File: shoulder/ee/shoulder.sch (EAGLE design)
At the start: 34 parts, among them IC3 XMEGA-A4, J1(RS) RJ11-6PTH, J2(LS) RJ11-6PTH, T1 2N2222

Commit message: shoulder: schematic updates for new board
- all through hole resistors replaced with 0603
- All through hole capacitors replaced with 0603
- through hole LEDs replaced with SMT
- Added jumpers to switch between SPI and USART peripheral for LED
  controllers
    - USART in SPI master mode allows DMA.
- Added reset button.
- Added a pullup on AVR reset line.
- Moved T1 and BUZZ (JST conn) further from screw holes.
- Moved vibrator further from screw holes.
- Replaced IR receivers with SMT heimdall package
- Added a footprint for a 3rd IR receiver (facing up)
- Replaced through hole NPN transistor with SMT
- Replaced 4 pin ISP with 6 pin 50mil RA header.
- Added frame to schematic :o
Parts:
- removed ISP1: (no value), SparkFun-Connectors:M04LOCK
- added C2: 0.1uF, SparkFun-Capacitors:CAP0603-CAP
- added ISP: PDI, greg:PDI
- added R1: (no value), SparkFun-Resistors:RESISTOR0603-RES
- added RST: SPST_TACT-EVQQ2, adafruit:SPST_TACT-EVQQ2
- added SJ1, SJ2: (no value), SparkFun-Passives:SOLDERJUMPER_2WAYT
- added U$3: TSMP77000UP, greg:TSMP77000UP
- C24, C25, C3, C4: device SparkFun-Passives:CAPPTH -> SparkFun-Capacitors:CAP0603-CAP
- R18, R19, R3, R4: device adafruit:R-US_0204/7 -> SparkFun-Resistors:RESISTOR0603-RES
- RGB1, RGB2, RGB3, RGB4, RGB5, RGB6, RGB7, RGB8: value RGBLED_CA-5MM -> AVAGO-RGB-SMT; device adafruit:RGBLED_CA-5MM -> greg:AVAGO-RGB-SMT
- T1: value 2N2222 -> (none); device adafruit:2N2222 -> SparkFun-DiscreteSemi:TRANSISTOR_NPNSOT23
- U$1, U$2: value PNA460XM -> TSMP77000SIDE; device adafruit:PNA460XM -> greg:TSMP77000SIDE
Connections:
- removed net N$4: IC3.PC5, LC2.STDI
- removed net N$7: IC3.RESET, ISP1.3
- new net LED-SCK: LC2.SCKI, SJ1.2
- new net LED-SCK/TXD: IC3.PC7, SJ1.3, SJ2.3
- new net LED-SDI: LC2.STDI, SJ2.2
- new net LED-XCK/SDO: IC3.PC5, SJ1.1, SJ2.1
- net +3V3: now also C2.2, U$3.VCC
- net GND: now also C2.1, ISP.GND, RST.P, RST.P1, U$3.GND; no longer ISP1.4
- net IRX-SH: now also U$3.OUT
- net N$5: now also IC3.RESET, ISP.CLK, R1.1, RST.S, RST.S1; no longer IC3.PC7, LC2.SCKI
- net N$6: now also ISP.DATA; no longer ISP1.2
- net N$9: now also ISP.VCC, R1.2; no longer ISP1.1
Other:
- note added: "IR receivers"
- note added: "Jump top two for USART in SPI master mode; jump bottom two for SPI"
- note added: "LED controllers"
- note added: "SPI to LED controllers"
- note added: "Vibrator"
- note added: "connection to front/back of vest"
- moved on the sheet: BUZZ, C1, C13, C16, C24, C25, C26, C27, C3, C4, C6, C7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

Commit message: Moved filter caps and added test points
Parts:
- added 3V3, GND, TP1, TP5, TP6, VSYS: PTR1PAD1-17, testpad:PTR1PAD1-17
- R1: value (none) -> 10k
- R3, R4: value (none) -> 2k4
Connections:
- net +3V3: now also 3V3.TP
- net +7V2: now also VSYS.TP
- net GND: now also GND.TP
- net IRX-SH: now also TP1.TP
- net LED-SCK: now also TP5.TP
- net LED-SDI: now also TP6.TP
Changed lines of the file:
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@@
 <setting verticaltext="up"/>
 </settings>
-<grid distance="25" unitdist="mil" unit="mil" style="lines" multiple="1" display="yes" altdistance="25" altunitdist="mil" altunit="mil"/>
+<grid distance="25" unitdist="mil" unit="mil" style="lines" multiple="1" display="yes" altdistance="25" altunitdist="inch" altunit="inch"/>
 <layers>
 <layer number="1" name="Top" color="4" fill="1" visible="no" active="no"/>
@@
 <part name="C24" library="SparkFun-Capacitors" deviceset="CAP" device="0603-CAP" value=".1uF"/>
 <part name="C25" library="SparkFun-Capacitors" deviceset="CAP" device="0603-CAP" value=".1uF"/>
-<part name="R4" library="SparkFun-Resistors" deviceset="RESISTOR" device="0603-RES"/>
-<part name="R3" library="SparkFun-Resistors" deviceset="RESISTOR" device="0603-RES"/>
+<part name="R4" library="SparkFun-Resistors" deviceset="RESISTOR" device="0603-RES" value="2k4"/>
+<part name="R3" library="SparkFun-Resistors" deviceset="RESISTOR" device="0603-RES" value="2k4"/>
 <part name="GND30" library="supply1" deviceset="GND" device=""/>
 <part name="GND31" library="supply1" deviceset="GND" device=""/>
@@
 <part name="BUZZ" library="adafruit" deviceset="JST_2PIN" device="-THM"/>
 <part name="GND1" library="supply1" deviceset="GND" device=""/>
-<part name="R1" library="SparkFun-Resistors" deviceset="RESISTOR" device="0603-RES"/>
+<part name="R1" library="SparkFun-Resistors" deviceset="RESISTOR" device="0603-RES" value="10k"/>
 <part name="RST" library="adafruit" deviceset="SPST_TACT" device="-EVQQ2"/>
 <part name="U$3" library="greg" deviceset="TSMP77000" device="UP"/>
@@
 <part name="ISP" library="greg" deviceset="PDI" device=""/>
 <part name="FRAME1" library="SparkFun-Aesthetics" deviceset="FRAME-A3" device=""/>
+<part name="TP1" library="testpad" deviceset="PTR1" device="PAD1-17"/>
+<part name="GND" library="testpad" deviceset="PTR1" device="PAD1-17"/>
+<part name="VSYS" library="testpad" deviceset="PTR1" device="PAD1-17"/>
+<part name="3V3" library="testpad" deviceset="PTR1" device="PAD1-17"/>
+<part name="TP5" library="testpad" deviceset="PTR1" device="PAD1-17">
+<attribute name="TP_SIGNAL_NAME" value=""/>
+</part>
+<part name="TP6" library="testpad" deviceset="PTR1" device="PAD1-17">
+<attribute name="TP_SIGNAL_NAME" value=""/>
+</part>
 </parts>
 <sheets>
@@
 <plain>
 <text x="71.12" y="149.86" size="1.778" layer="94">Jump top two for USART in SPI master mode; jump bottom two for SPI</text>
-<text x="-178.435" y="173.355" size="5.08" layer="94">connection to front/back of vest</text>
+<text x="-165.735" y="167.64" size="5.08" layer="94">connection to front/back of vest</text>
 <text x="64.77" y="193.675" size="5.08" layer="94">IR receivers</text>
 <text x="-22.225" y="172.72" size="5.08" layer="94">Vibrator</text>
@@
 <instance part="J2(LS)" gate="G$1" x="-59.055" y="196.215" rot="MR0"/>
 <instance part="GND11" gate="1" x="-122.555" y="183.515"/>
-<instance part="U$15" gate="G$1" x="-89.535" y="186.055" rot="MR90"/>
-<instance part="+3V2" gate="G$1" x="-150.495" y="186.055" rot="R90"/>
+<instance part="U$15" gate="G$1" x="-80.645" y="186.055" rot="MR90"/>
+<instance part="+3V2" gate="G$1" x="-158.115" y="186.055" rot="R90"/>
 <instance part="RGB4" gate="G$1" x="30.48" y="117.475"/>
 <instance part="RGB3" gate="G$1" x="30.48" y="94.615"/>
@@
 <instance part="ISP" gate="G$1" x="-158.75" y="94.615" rot="R270"/>
 <instance part="FRAME1" gate="G$1" x="-208.28" y="-17.78"/>
+<instance part="TP1" gate="G$1" x="125.73" y="193.04" rot="R90"/>
+<instance part="GND" gate="G$1" x="-120.015" y="189.23" rot="R90"/>
+<instance part="VSYS" gate="G$1" x="-93.98" y="182.88"/>
+<instance part="3V3" gate="G$1" x="-147.32" y="182.245"/>
+<instance part="TP5" gate="G$1" x="76.2" y="170.18" rot="R270"/>
+<instance part="TP6" gate="G$1" x="129.54" y="170.18" rot="R90"/>
 </instances>
 <busses>
@@
 <wire x1="-168.275" y1="193.675" x2="-122.555" y2="193.675" width="0.1524" layer="91"/>
 <wire x1="-122.555" y1="193.675" x2="-64.135" y2="193.675" width="0.1524" layer="91"/>
-<wire x1="-122.555" y1="193.675" x2="-122.555" y2="186.055" width="0.1524" layer="91"/>
+<wire x1="-122.555" y1="193.675" x2="-122.555" y2="189.23" width="0.1524" layer="91"/>
 <junction x="-122.555" y="193.675"/>
 <pinref part="C6" gate="G$1" pin="1"/>
+<wire x1="-122.555" y1="189.23" x2="-122.555" y2="186.055" width="0.1524" layer="91"/>
 <wire x1="-132.715" y1="186.055" x2="-122.555" y2="186.055" width="0.1524" layer="91"/>
 <junction x="-122.555" y="186.055"/>
@@
 <wire x1="-122.555" y1="198.755" x2="-168.275" y2="198.755" width="0.1524" layer="91"/>
 <junction x="-122.555" y="198.755"/>
+<pinref part="GND" gate="G$1" pin="TP"/>
+<junction x="-122.555" y="189.23"/>
 </segment>
 <segment>
@@
 <wire x1="113.03" y1="201.295" x2="85.09" y2="201.295" width="0.1524" layer="91"/>
 <junction x="113.03" y="201.295"/>
-<wire x1="113.03" y1="201.295" x2="113.03" y2="193.675" width="0.1524" layer="91"/>
+<wire x1="113.03" y1="201.295" x2="113.03" y2="193.04" width="0.1524" layer="91"/>
 <label x="113.03" y="193.675" size="1.778" layer="95"/>
 <pinref part="U$3" gate="G$1" pin="OUT"/>
 <wire x1="140.97" y1="201.295" x2="140.97" y2="219.075" width="0.1524" layer="91"/>
 <wire x1="113.03" y1="201.295" x2="140.97" y2="201.295" width="0.1524" layer="91"/>
-<wire x1="113.03" y1="193.675" x2="123.19" y2="193.675" width="0.1524" layer="91"/>
+<wire x1="113.03" y1="193.04" x2="123.19" y2="193.04" width="0.1524" layer="91"/>
+<pinref part="TP1" gate="G$1" pin="TP"/>
 </segment>
 </net>
@@
 <pinref part="U$15" gate="G$1" pin="+7V2"/>
 <pinref part="C7" gate="G$1" pin="2"/>
-<wire x1="-102.235" y1="186.055" x2="-92.075" y2="186.055" width="0.1524" layer="91"/>
+<wire x1="-102.235" y1="186.055" x2="-93.98" y2="186.055" width="0.1524" layer="91"/>
 <junction x="-102.235" y="186.055"/>
+<pinref part="VSYS" gate="G$1" pin="TP"/>
+<wire x1="-93.98" y1="186.055" x2="-83.185" y2="186.055" width="0.1524" layer="91"/>
+<wire x1="-93.98" y1="185.42" x2="-93.98" y2="186.055" width="0.1524" layer="91"/>
+<junction x="-93.98" y="186.055"/>
 </segment>
 </net>
@@
 <junction x="-140.335" y="196.215"/>
 <pinref part="C6" gate="G$1" pin="2"/>
-<wire x1="-140.335" y1="186.055" x2="-147.955" y2="186.055" width="0.1524" layer="91"/>
+<wire x1="-140.335" y1="186.055" x2="-147.32" y2="186.055" width="0.1524" layer="91"/>
 <junction x="-140.335" y="186.055"/>
+<pinref part="3V3" gate="G$1" pin="TP"/>
+<wire x1="-147.32" y1="186.055" x2="-155.575" y2="186.055" width="0.1524" layer="91"/>
+<wire x1="-147.32" y1="184.785" x2="-147.32" y2="186.055" width="0.1524" layer="91"/>
+<junction x="-147.32" y="186.055"/>
 </segment>
 <segment>
@@
 <pinref part="SJ1" gate="G$1" pin="2"/>
 <label x="81.28" y="170.18" size="1.778" layer="95"/>
+<pinref part="TP5" gate="G$1" pin="TP"/>
 </segment>
 </net>
@@
 <pinref part="SJ2" gate="G$1" pin="2"/>
 <label x="114.3" y="170.18" size="1.778" layer="95"/>
-</segment>
-</net>
+<pinref part="TP6" gate="G$1" pin="TP"/>
+</segment>
+</net>

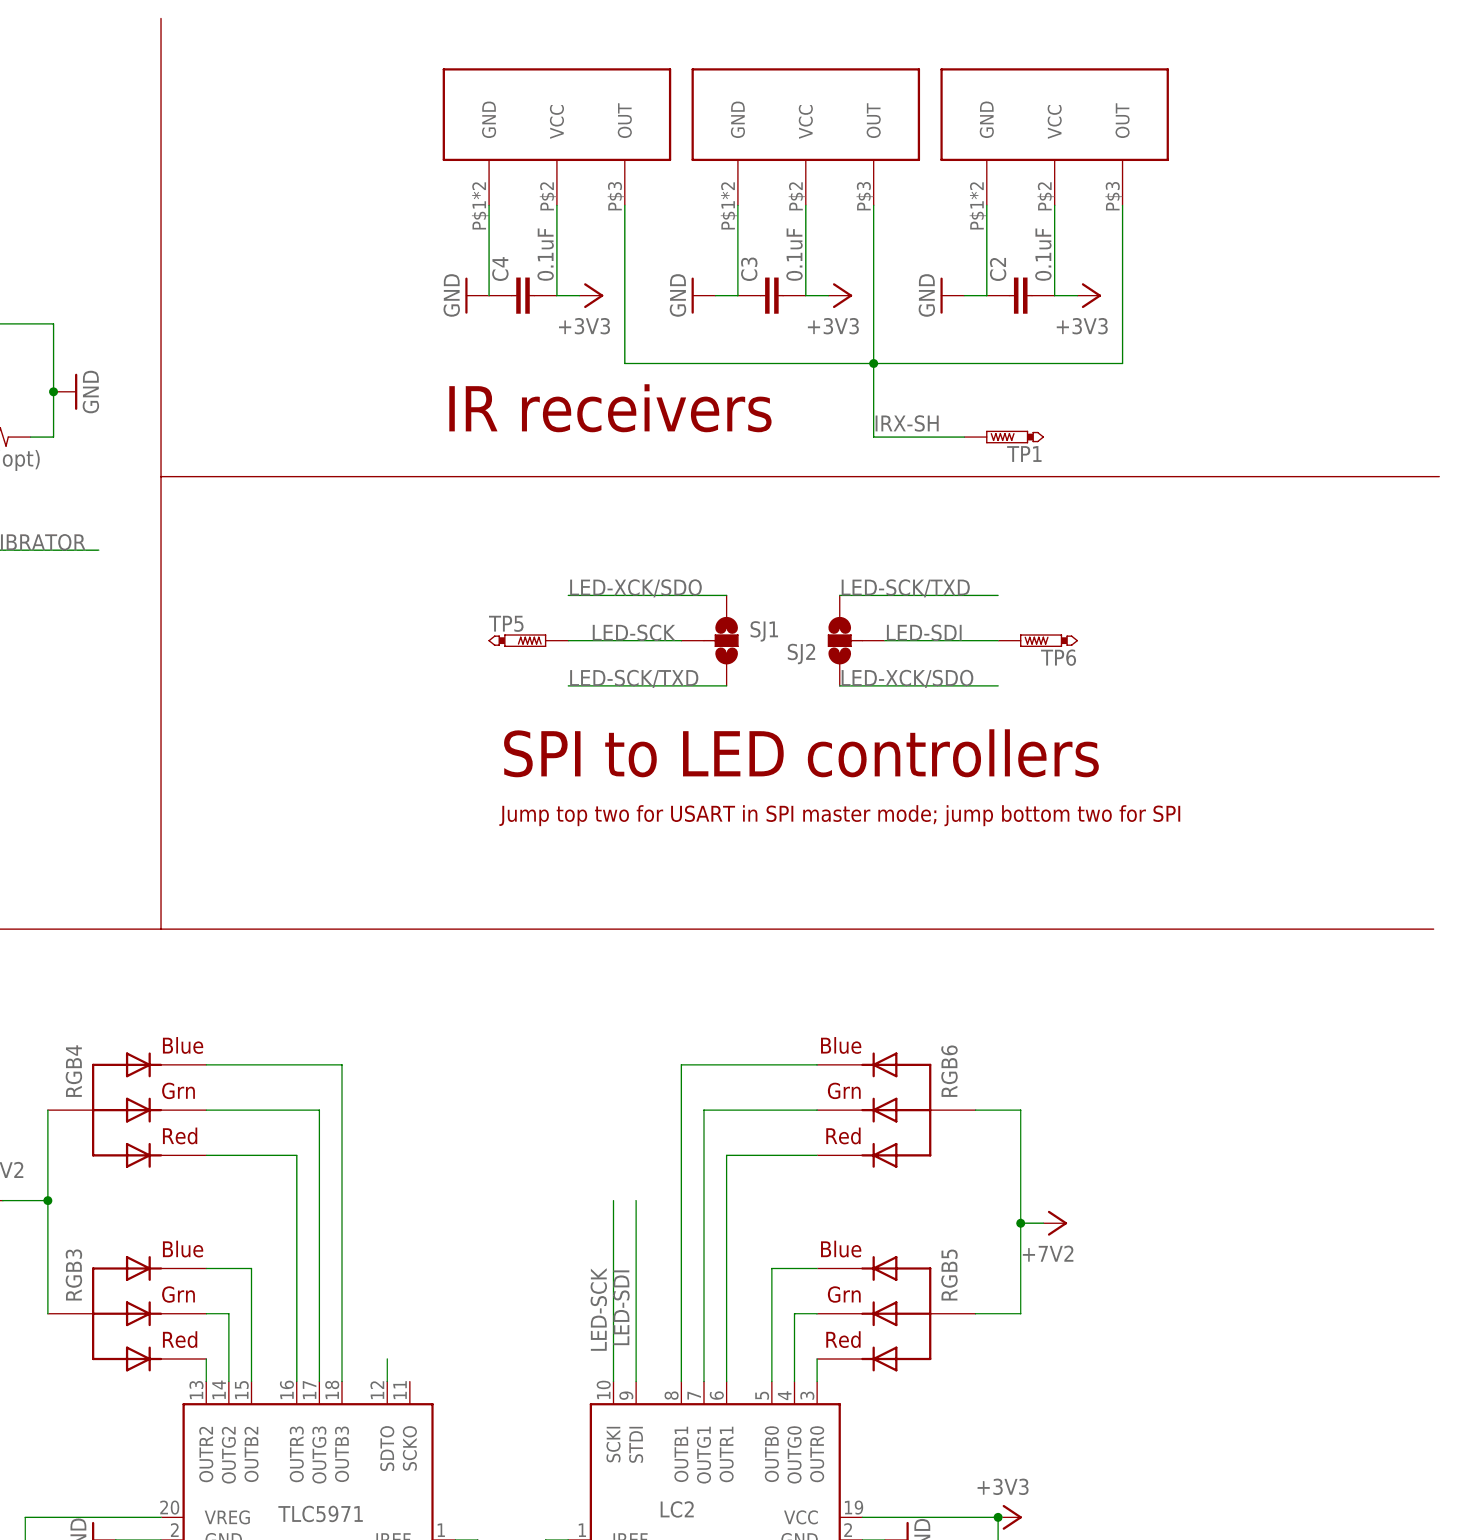
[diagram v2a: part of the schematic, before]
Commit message: shoulder board: fix rev2 bugs
- Bump board revision to rev3
- Remove USART/SPI jumper - USART works fine
    - resolves GF-38
- Fix ISP pin hole sizing
    - resolves GF-37
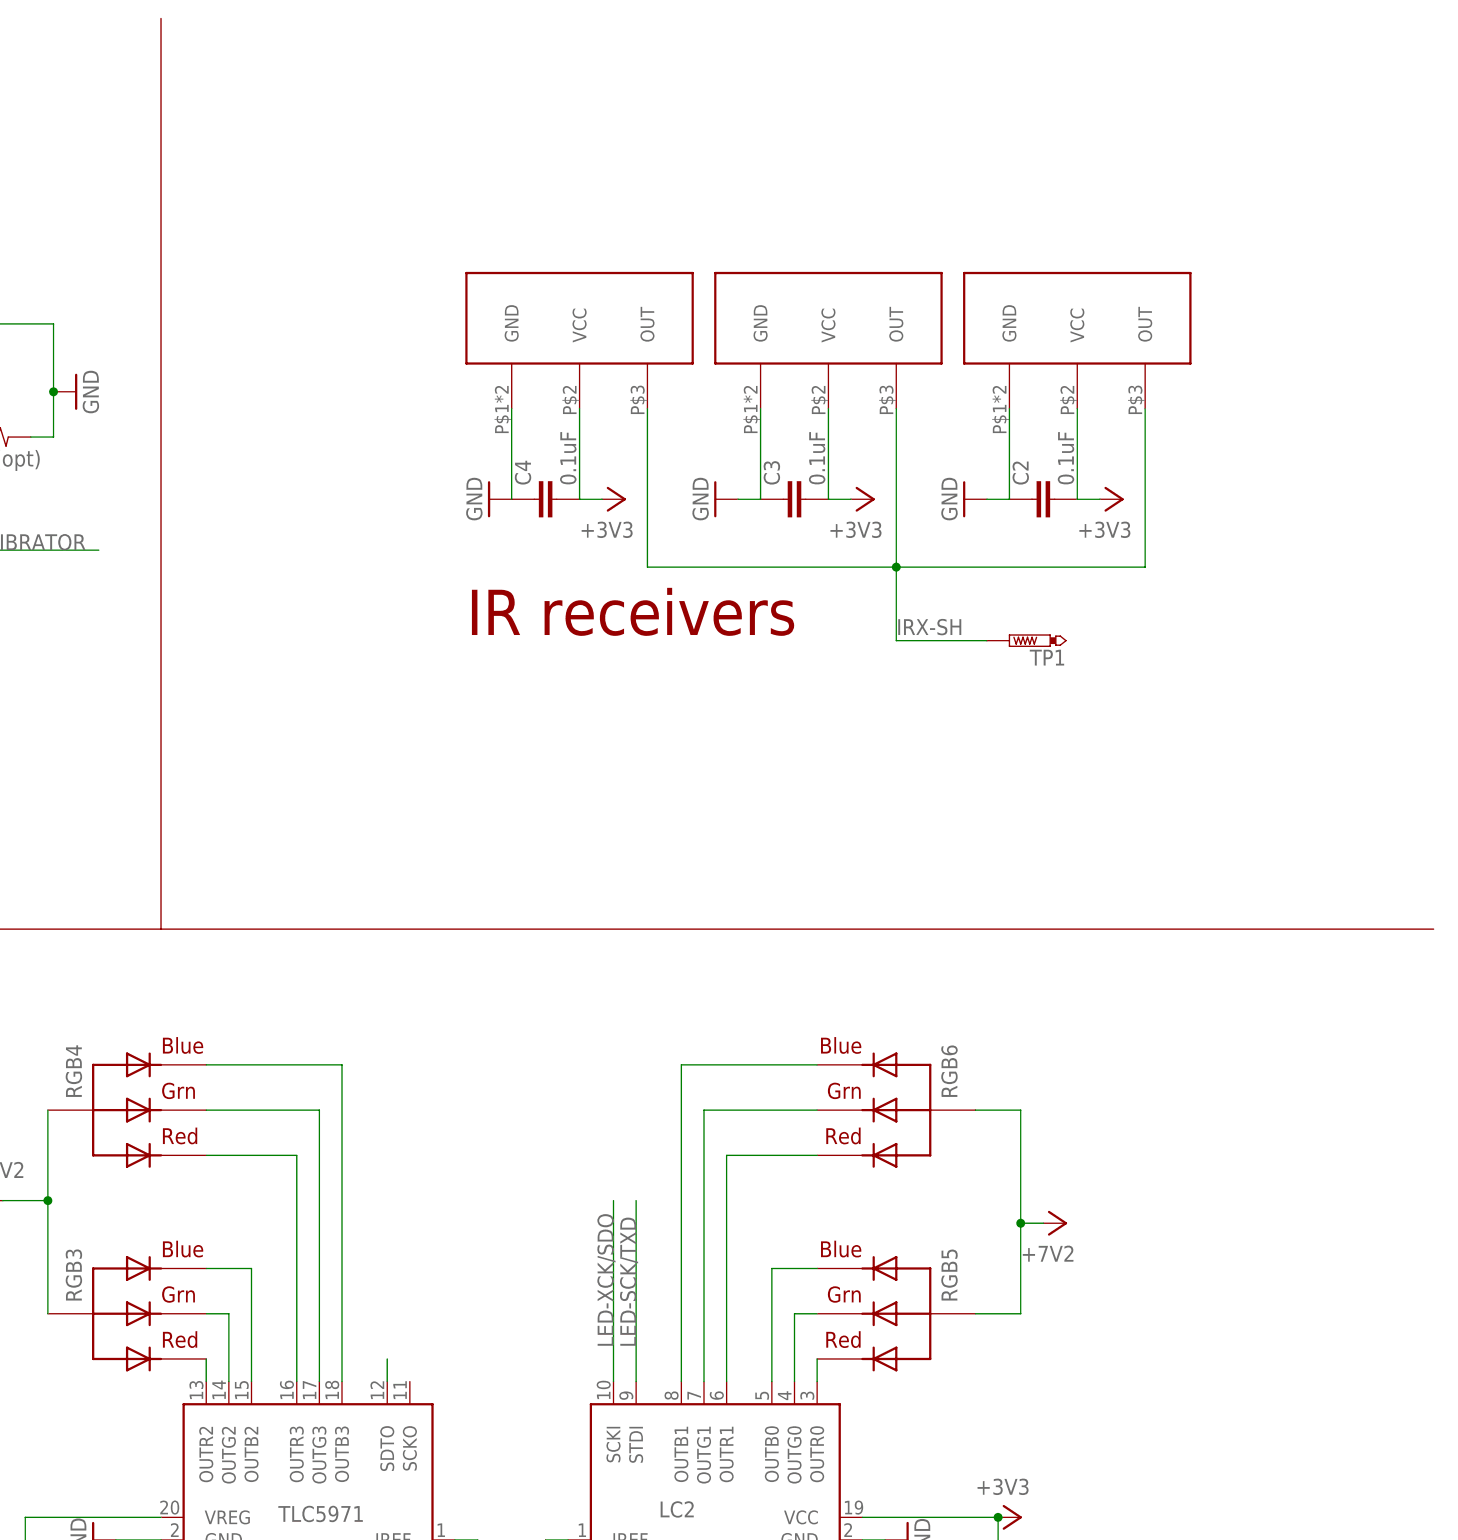
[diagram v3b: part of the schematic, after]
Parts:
- removed SJ1, SJ2: (no value), SparkFun-Passives:SOLDERJUMPER_2WAYT
- removed TP5, TP6: PTR1PAD1-17, testpad:PTR1PAD1-17
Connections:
- removed net LED-SCK: LC2.SCKI, SJ1.2, TP5.TP
- removed net LED-SDI: LC2.STDI, SJ2.2, TP6.TP
- net LED-SCK/TXD: now also LC2.STDI; no longer SJ1.3, SJ2.3
- net LED-XCK/SDO: now also LC2.SCKI; no longer SJ1.1, SJ2.1
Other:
- note removed: "Jump top two for USART in SPI master mode; jump bottom two for SPI"
- note removed: "SPI to LED controllers"
- moved on the sheet: C2, C3, C4, TP1

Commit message: Shoulder rev4 hardware
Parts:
- removed C13, C16, C26, C27: 100nF, SparkFun-Passives:CAP0603-CAP
- removed IC3: XMEGA-A4, xmega:AVR_XMEGA_A4_44A
- removed ISP: PDI, greg:PDI
- added C10, C11, C12, C9: 100nF, SparkFun-Passives:CAP0603-CAP
- added C5: 10uF, SparkFun-Passives:CAP0603-CAP
- added C8: 1uF, SparkFun-Passives:CAP0603-CAP
- added JP1: CORTEX_DEBUGPTH, greg:CORTEX_DEBUGPTH
- added L2: (no value), SparkFun-Passives:INDUCTOR0603
- added L3: 10uH, SparkFun-Passives:INDUCTOR0805
- added R2: 1k, SparkFun-Resistors:RESISTOR0603-RES
- added R5: 330, SparkFun-Resistors:RESISTOR0603-RES
- added U1: ATSAML21E-A, greg:ATSAML21E-A
- C1: device SparkFun-Passives:CAP1206 -> SparkFun-Passives:CAP0603-CAP
- L1: value (none) -> 10uH; device greg:INDUCTOR1206H* -> SparkFun-Passives:INDUCTOR0805
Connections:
- removed net N$9: C1.2, C13.2, C16.2, C26.2, C27.2, IC3.AVCC, IC3.VCC1, IC3.VCC2, IC3.VCC3, ISP.VCC, L1.2, R1.2
- new net N$12: C8.1, C9.1, L1.1, U1.VDDCORE
- new net N$4: C10.2, C5.2, L2.1, U1.VDDANA
- new net N$7: L1.2, U1.VSW
- new net RST: C12.2, JP1.NRESET, R1.1, R5.1, U1.!RESET!
- new net SWCLK: JP1.SWDCLK/TCK, R2.2, U1.PA30(SWCLK/SER1:2+)
- new net SWDIO: JP1.SWDIO/TMS, U1.PA31(SWDIO/SER1:3+)
- net +3V3: now also JP1.VCC, L3.1, R1.2, R2.1; no longer L1.1
- net GND: now also C10.1, C11.1, C12.1, C5.1, C8.2, C9.2, JP1.GND@3, JP1.GND@5, U1.GND; no longer C13.1, C16.1, C26.1, C27.1, IC3.AGND, IC3.GND1, IC3.GND2, IC3.GND3, ISP.GND
- net IRX-SH: now also U1.PA08(I2C/AIN16/SER0:0+); no longer IC3.PE2
- net LED-SCK/TXD: now also U1.PA04(AIN4/REFB/SER0:0/TC0:0); no longer IC3.PC7
- net LED-XCK/SDO: now also U1.PA05(AIN5/SER0:1/TC0:1); no longer IC3.PC5
- net LIGHTS-SCL: now also U1.PA17(I2C/SER1:1+), U1.PA23(I2C/SER3:1+); no longer IC3.PC1
- net LIGHTS-SDA: now also U1.PA16(I2C/SER1:0+), U1.PA22(I2C/SER3:0+); no longer IC3.PC0
- net N$5: now also C1.2, C11.2, L2.2, L3.2, U1.VDDIN; no longer IC3.RESET, ISP.CLK, R1.1, RST.S, RST.S1
- net N$6: now also R5.2, RST.S, RST.S1; no longer IC3.PDI_DATA, ISP.DATA
- net VIBRATOR: now also U1.PA27; no longer IC3.PA3
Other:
- note added: "SERCOM0"
- note added: "SERCOM1"
- note added: "SERCOM2"
- note added: "SERCOM3"
- moved on the sheet: C1, L1, R1, RST
